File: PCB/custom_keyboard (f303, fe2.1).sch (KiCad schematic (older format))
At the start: 423 parts, among them IC1 FE2.1, J2 Conn_01x03_Male, J5 AVR-ISP-6, Q1 DTC123J, SW1 SW_Push, U1 24LC02BT-I/SN, U10 PRTR5V0U2X, U11 XC6206P332MR, U12 74LVC1G34, U13 XC6206P332MR, U2 PRTR5V0U2X, U3 PRTR5V0U2X, U4 PRTR5V0U2X, U5 PRTR5V0U2X, U6 PRTR5V0U2X, U7 PRTR5V0U2X, U8 PRTR5V0U2X, U9 STM32F303CBT6, Y1 8MHz, Y2 32.768KHz, Y3 12MHz

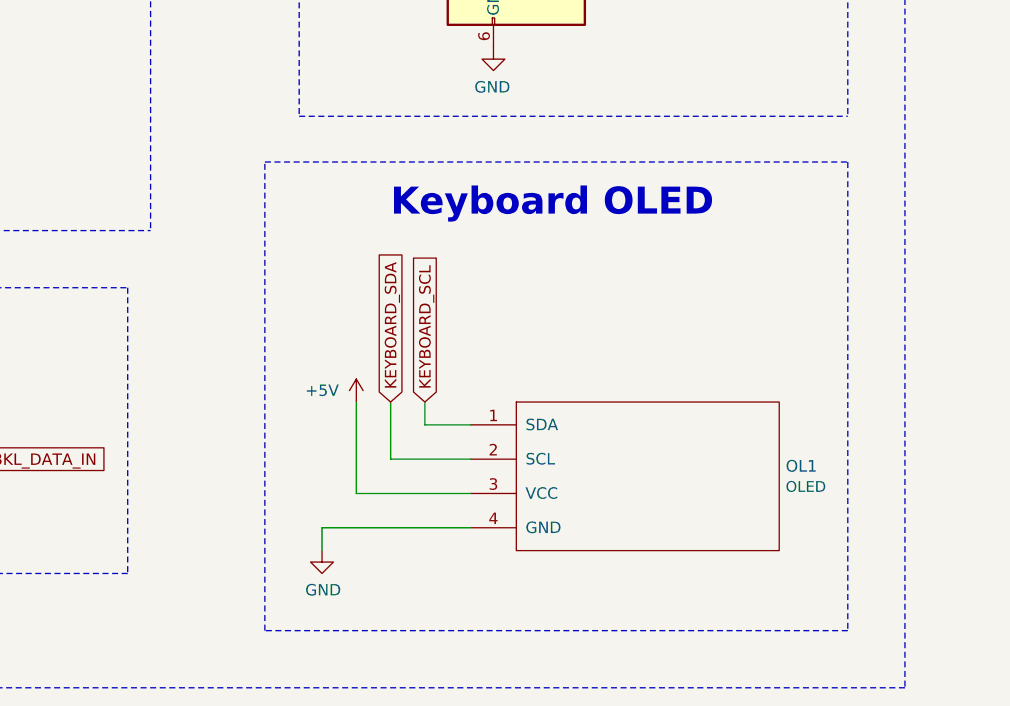
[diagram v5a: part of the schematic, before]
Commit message: Added pullup resistors for oled
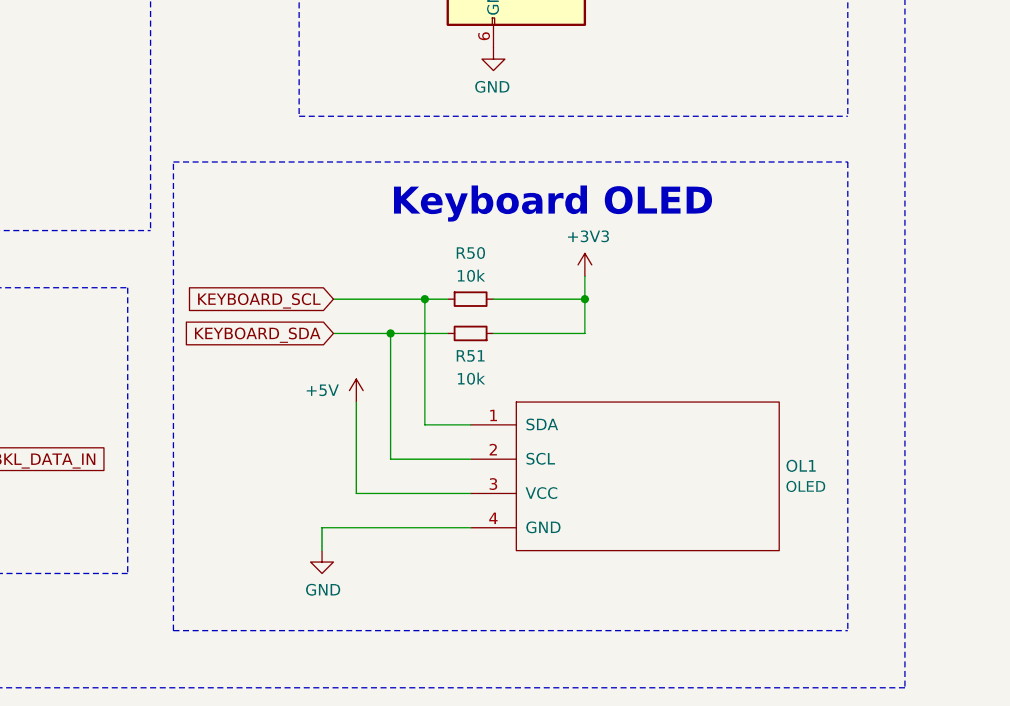
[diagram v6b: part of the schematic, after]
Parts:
- added R50, R51: 10k, Resistor_SMD:R_0603_1608Metric, symbol Device:R_Small
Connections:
- net +3V3: now also R50.2, R51.1
- net KEYBOARD_SCL: now also R50.1
- net KEYBOARD_SDA: now also R51.2
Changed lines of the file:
@@
 	1    0    0    -1
 $EndComp
-$Comp
-L power:+3V3 #PWR0189
-U 1 1 94B509E6
-P 5200 20900
-F 0 "#PWR0189" H 5200 20750 50  0001 C CNN
-F 1 "+3V3" H 5215 21073 50  0000 C CNN
-F 2 "" H 5200 20900 50  0001 C CNN
-F 3 "" H 5200 20900 50  0001 C CNN
-	1    5200 20900
-	1    0    0    -1
-$EndComp
 Wire Wire Line
 	5200 21000 5000 21000
@@
 	1    0    0    -1
 $EndComp
-Text GLabel 9450 20800 1    50   Input ~ 0
+Text GLabel 9200 20500 0    50   Input ~ 0
 KEYBOARD_SDA
-Text GLabel 9600 20800 1    50   Input ~ 0
+Text GLabel 9200 20350 0    50   Input ~ 0
 KEYBOARD_SCL
 $Comp
@@
 Keyboard OLED
 Wire Wire Line
-	9600 20800 9600 20900
-Wire Wire Line
 	9300 20800 9300 21200
 Wire Wire Line
-	9450 21050 9450 20800
-Wire Wire Line
 	9150 21450 9150 21350
 Wire Notes Line
 	11450 19750 11450 21800
 Wire Notes Line
-	11450 21800 8900 21800
-Wire Notes Line
-	8900 21800 8900 19750
-Wire Notes Line
-	8900 19750 11450 19750
+	8500 21800 8500 19750
 Wire Notes Line
 	9150 13850 11450 13850
@@
 Wire Wire Line
 	9550 17100 9700 17100
+Wire Wire Line
+	9200 20500 9450 20500
+Wire Wire Line
+	9200 20350 9600 20350
+$Comp
+L power:+3V3 #PWR0189
+U 1 1 94B509E6
+P 5200 20900
+F 0 "#PWR0189" H 5200 20750 50  0001 C CNN
+F 1 "+3V3" H 5215 21073 50  0000 C CNN
+F 2 "" H 5200 20900 50  0001 C CNN
+F 3 "" H 5200 20900 50  0001 C CNN
+	1    5200 20900
+	1    0    0    -1
+$EndComp
+$Comp
+L power:+3V3 #PWR0289
+U 1 1 64966A39
+P 10300 20250
+F 0 "#PWR0289" H 10300 20100 50  0001 C CNN
+F 1 "+3V3" H 10315 20423 50  0000 C CNN
+F 2 "" H 10300 20250 50  0001 C CNN
+F 3 "" H 10300 20250 50  0001 C CNN
+	1    10300 20250
+	1    0    0    -1
+$EndComp
+Wire Wire Line
+	9600 20350 9700 20350
+Connection ~ 9600 20350
+Wire Wire Line
+	9450 20500 9700 20500
+Connection ~ 9450 20500
+Wire Wire Line
+	10300 20500 10300 20350
+Wire Wire Line
+	9900 20350 10300 20350
+Connection ~ 10300 20350
+Wire Wire Line
+	10300 20350 10300 20250
+$Comp
+L Device:R_Small R51
+U 1 1 66F399AC
+P 9800 20500
+F 0 "R51" V 9700 20500 50  0000 C CNN
+F 1 "10k" V 9600 20500 50  0000 C CNN
+F 2 "Resistor_SMD:R_0603_1608Metric" H 9800 20500 50  0001 C CNN
+F 3 "~" H 9800 20500 50  0001 C CNN
+	1    9800 20500
+	0    1    -1   0
+$EndComp
+Wire Wire Line
+	9900 20500 10300 20500
+Wire Wire Line
+	9450 20500 9450 21050
+Wire Wire Line
+	9600 20350 9600 20900
+Wire Notes Line
+	8500 19750 11450 19750
+Wire Notes Line
+	8500 21800 11450 21800
+$Comp
+L Device:R_Small R50
+U 1 1 69B93952
+P 9800 20350
+F 0 "R50" V 9600 20350 50  0000 C CNN
+F 1 "10k" V 9700 20350 50  0000 C CNN
+F 2 "Resistor_SMD:R_0603_1608Metric" H 9800 20350 50  0001 C CNN
+F 3 "~" H 9800 20350 50  0001 C CNN
+	1    9800 20350
+	0    -1   1    0
+$EndComp
 $EndSCHEMATC
